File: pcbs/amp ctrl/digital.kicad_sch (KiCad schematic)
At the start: 93 parts

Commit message: Schematic file fix, misc. PCB
Fixed issue with KiCAD's automatic V5→V6 migration (corrected in 6.0.11) that caused problems with component references in multi-channel schematic sheets
Finished migration in amp ctrl PCB, inc. re-assigning "exclude from BOM" attributes to testpoints, solder jumpers
Added mounting hole to amp ctrl PCB for addl support to Ethernet jacks, power connector through stiffener
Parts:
- JP71, TP22, TP23, TP24, TP25, TP26, TP27, TP28, TP29, TP31, TP42, TP43, TP44, TP45, TP46, TP47, TP48, TP49: renamed from ?; now left out of the parts list
- gave numbers to parts that had none: 75

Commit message: New CS amp, misc. layout
Changed current sense amp from INA828 to INA821/819 due to availability: schematic, layout for channel 1 (#6)
Moved some thermistor components & ~Shutdown cap out of the way of the stiffener (#3)
Updated footprints: SOD-323F for slightly larger solderable pads, SOIC-8 to remove excessive length on inside edge
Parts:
- U90: Type (none) -> SMT
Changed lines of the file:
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@@
+      (effects (font (size 1.27 1.27)) hide)
+    )
+    (property "Type" "SMT" (id 8) (at 327.66 158.75 0)
       (effects (font (size 1.27 1.27)) hide)
     )

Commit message: New DAC
Changed DAC from LTC2656 to AD5676 (#5)
Changed digital Vdd for ADC to +3.3V
Removed level translator ICs for +3.3V to +5V; no longer needed because AD5676 has separate analog and digital supply pins
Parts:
- removed JP71: Jumper_NC_Small, Jumper:SolderJumper-2_P1.3mm_Bridged_RoundedPad1.0x1.5mm, symbol amp-ctrl-rescue:Jumper_NC_Small-Device
- removed U8: LTC2656, Martinos:SSOP-20-1EP_4.4x6.5mm_P0.65mm, symbol amp-ctrl-rescue:LTC2656-Martinos
- added C202: 1uF 16V X7R, Capacitor_SMD:C_0603_1608Metric, symbol Device:C
- added R288: 0, Resistor_SMD:R_0805_2012Metric, symbol Device:R
- added U8: AD5676, Don_std:TSSOP-20_4.4x6.5mm_P0.65mm, symbol Don:AD567x
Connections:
- net +5V: no longer C57.2, U90.30 (DVdd)
- net DAC_MISO: now also U8.16 (SDO)
- net DAC_MOSI: now also U8.7 (SDI)
- net DAC_SCKI: now also U8.6 (SCLK)
- net GND: now also C202.1, U8.13 (GND)
- net Vref_Buffered: now also R288.1
- net ~{DAC_CS}: now also U8.5 (~{SYNC})
- net ~{LDAC}: now also U8.15 (~{LDAC})
- net ~{Reset}: now also U8.17 (~{RESET})
- net at R30.1, TP26.1: now also U8.12 (Vout4)
- net at R31.1, TP27.1: now also U8.11 (Vout5)
- net at R32.1, TP28.1: now also U8.10 (Vout6)
- net at R33.1, TP29.1: now also U8.9 (Vout7)
- net at R26.1, TP22.1: now also U8.2 (Vout0)
- net at R27.1, TP23.1: now also U8.1 (Vout1)
- net at R28.1, TP24.1: now also U8.20 (Vout2)
- net at R29.1, TP25.1: now also U8.19 (Vout3)
- net DAC_VCC: no longer names the net of C27.2, C28.2, R21.2
- net DAC_VCC: now also U8.3 (VDD)
- new net: R288.2, U8.18 (VREF)
- new net +3V3: C202.2, C57.2, U8.14 (RSTSEL), U8.4 (VLOGIC), U8.8 (GAIN), U90.30 (DVdd)
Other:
- note added: "GAIN = 1: range is from 0 to 2*Vref RSTSEL = 1: powers up to mid-scale (0A) VREF series resistor allows adding series resistance in case the AD5676R needs to be used due to availability, to limit current draw while the external op-amp and internal Vref buffer "fight" until the internal Vref can be disabled"
- note removed: "PORSEL=1: Resets to mid-scale (0A out) on power-up"
- moved on the sheet: C27, C28, R21

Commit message: DRC fixes
Deleted track stubs and overlapping vias, other misc. DRC fixes (#3)
Shrank width of SOT-563 pads to fall within 0.16 mm clearance (6.3 mils)
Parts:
- J14: footprint Martinos:Shield_Wurth_36107406S_Minimal-inside -> Don:Shield_Wurth_36107406S_Minimal-inside
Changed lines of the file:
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@@
       (effects (font (size 1.27 1.27)) (justify left) hide)
     )
-    (property "Footprint" "Martinos:Shield_Wurth_36107406S_Minimal-inside" (id 2) (at 201.93 120.65 0)
+    (property "Footprint" "Don:Shield_Wurth_36107406S_Minimal-inside" (id 2) (at 201.93 120.65 0)
       (effects (font (size 1.27 1.27)) hide)
     )
@@
   (symbol (lib_id "amp-ctrl-rescue:+3.3V-power") (at 21.59 97.79 90) (mirror x) (unit 1)
     (in_bom yes) (on_board yes)
-    (property "Reference" "#PWR?" (id 0) (at 25.4 97.79 0)
-      (effects (font (size 1.27 1.27)) hide)
-    )
+    (property "Reference" "#PWR0553" (id 0) (at 25.4 97.79 0)
+      (effects (font (size 1.27 1.27)) hide)
+    )

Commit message: Manufacturing fixes for amp control board
Arranged *.Fab text for assembly drawings
Minor stiffener outline fixes, silkscreen fixes
Fixed missing BOM fields on some parts
Removed exported manufacturing files from version control
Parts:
- C26, C31: Manufacturer (none) -> Murata; Part Number (none) -> GRM1885C1H122JA01J
- U6: Type (none) -> SMT
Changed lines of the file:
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@@
   (title_block
     (title "Digital Controls and Voltage Reference")
-    (rev "D3")
+    (date "2023-05-04")
+    (rev "D4")
     (company "Martinos Center @ MGH")
     (comment 1 "Don Straney")
@@
       (effects (font (size 1.27 1.27)) hide)
     )
+    (property "Type" "SMT" (id 8) (at 312.42 96.52 0)
+      (effects (font (size 1.27 1.27)) hide)
+    )
     (pin "1")
     (pin "2")
@@
       (effects (font (size 1.27 1.27)) hide)
     )
-    (property "Manufacturer" "" (id 5) (at 351.79 121.92 0)
+    (property "Manufacturer" "Murata" (id 5) (at 351.79 121.92 0)
       (effects (font (size 1.27 1.27)) hide)
     )
-    (property "Part Number" "" (id 6) (at 351.79 121.92 0)
+    (property "Part Number" "GRM1885C1H122JA01J" (id 6) (at 351.79 121.92 0)
       (effects (font (size 1.27 1.27)) hide)
     )
@@
       (effects (font (size 1.27 1.27)) hide)
     )
-    (property "Manufacturer" "" (id 5) (at 351.79 100.33 0)
+    (property "Manufacturer" "Murata" (id 5) (at 351.79 100.33 0)
       (effects (font (size 1.27 1.27)) hide)
     )
-    (property "Part Number" "" (id 6) (at 351.79 100.33 0)
+    (property "Part Number" "GRM1885C1H122JA01J" (id 6) (at 351.79 100.33 0)
       (effects (font (size 1.27 1.27)) hide)
     )

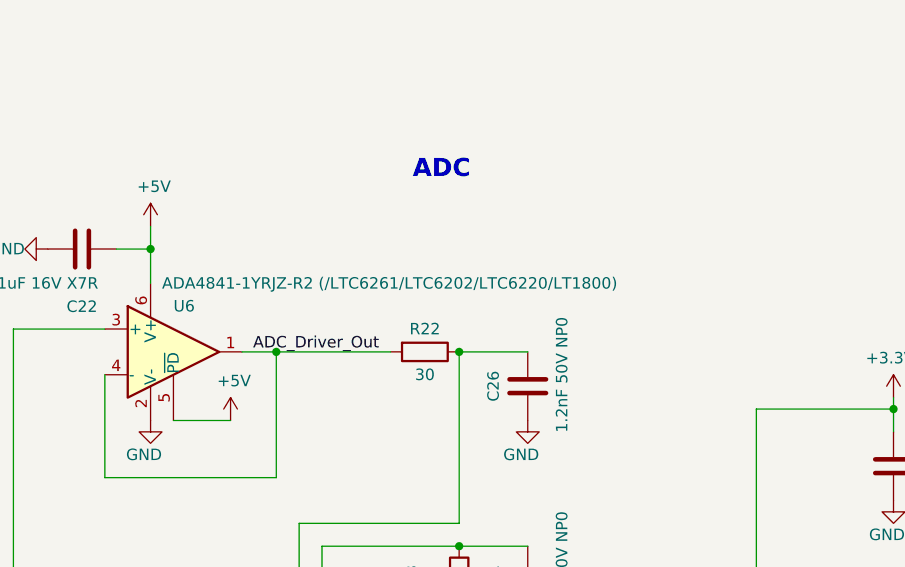
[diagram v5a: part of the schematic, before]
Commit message: Corrected amp board ADC op-amp, created ODU connector 6x7 board
Pared down list of ADC driver op-amps to list of ones tested
Minor fixes to ODU 6x7 connector board (forward-pinned)
Created duplicate of ODU 6x7 connector board, for reverse-pinned
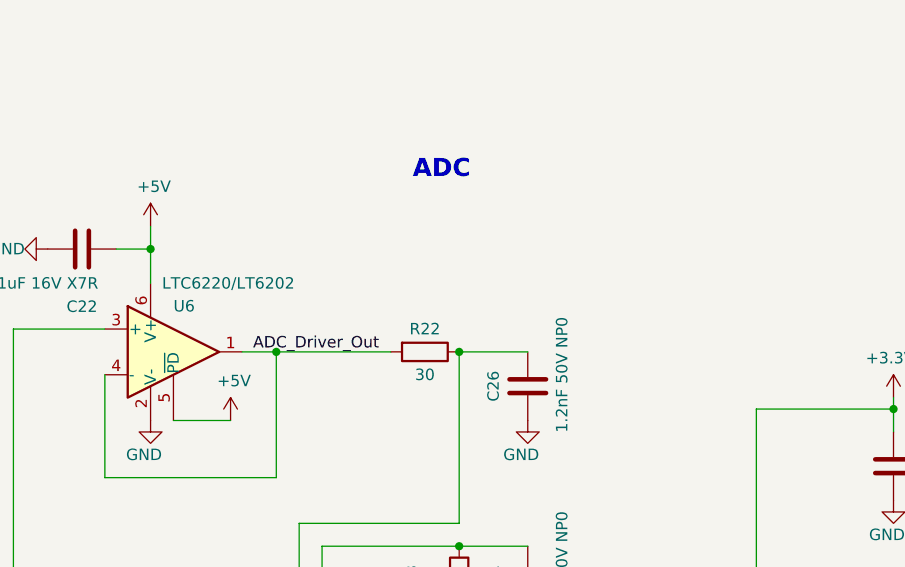
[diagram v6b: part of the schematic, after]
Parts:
- U6: value ADA4841-1YRJZ-R2 (/LTC6261/LTC6202/LTC6220/LT1800) -> LTC6220/LT6202; Part Number ADA4841-1YRJZ-R2 -> LT6220CS5#TRMPBF; Part Number Alt. ADA4841-1YRJZ-R7, LTC6261IS6#TRMPBF, LTC6261HS6#TRMPBF, LTC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 -> LT6220CS5#TRPBF, LT6220IS5#TRMPBF, LT6202HS5#TRMPBF, LT6202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
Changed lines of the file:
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@@
       (effects (font (size 1.27 1.27)) (justify left))
     )
-    (property "Value" "ADA4841-1YRJZ-R2 (/LTC6261/LTC6202/LTC6220/LT1800)" (id 1) (at 311.15 88.9 0)
+    (property "Value" "LTC6220/LT6202" (id 1) (at 311.15 88.9 0)
       (effects (font (size 1.27 1.27)) (justify left))
     )
@@
       (effects (font (size 1.27 1.27)) hide)
     )
-    (property "Part Number" "ADA4841-1YRJZ-R2" (id 5) (at 312.42 96.52 0)
+    (property "Part Number" "LT6220CS5#TRMPBF" (id 5) (at 312.42 96.52 0)
       (effects (font (size 1.27 1.27)) hide)
     )
@@
       (effects (font (size 1.27 1.27)) hide)
     )
-    (property "Part Number Alt." "ADA4841-1YRJZ-R7, LTC6261IS6#TRMPBF, LTC6261HS6#TRMPBF, LTC6261CS6#TRMPBF, LT6202HS5#TRMPBF, LT6202CS5#TRMPBF, LT6202IS5#TRPBF, LT6202IS5#TRMPBF, LT6220CS5#TRMPBF, LT6220CS5#TRPBF, LT6220IS5#TRMPBF, LT1800CS5#TRMPBF, LT1800IS5#TRMPBF, LT1800IS5#TRPBF, LT1800CS5#TRPBF" (id 7) (at 312.42 96.52 0)
+    (property "Part Number Alt." "LT6220CS5#TRPBF, LT6220IS5#TRMPBF, LT6202HS5#TRMPBF, LT6202CS5#TRMPBF, LT6202IS5#TRPBF, LT6202IS5#TRMPBF" (id 7) (at 312.42 96.52 0)
       (effects (font (size 1.27 1.27)) hide)
     )

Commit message: Misc. mfg
Marked top-side testpoints on amp control board as DNP
Updated serial interface board's BOM-placement-help file
Exported stiffener file for amp control board
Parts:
- TP30, TP32, TP60, TP61: DNP (none) -> DNP
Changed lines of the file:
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@@
+      (effects (font (size 1.27 1.27)) hide)
+    )
+    (property "DNP" "DNP" (id 7) (at 363.22 215.9 0)
       (effects (font (size 1.27 1.27)) hide)
     )
@@
     )
     (property "Part Number" "5019" (id 6) (at 374.65 215.9 0)
+      (effects (font (size 1.27 1.27)) hide)
+    )
+    (property "DNP" "DNP" (id 7) (at 374.65 215.9 0)
       (effects (font (size 1.27 1.27)) hide)
     )
@@
       (effects (font (size 1.27 1.27)) hide)
     )
+    (property "DNP" "DNP" (id 7) (at 153.67 153.67 0)
+      (effects (font (size 1.27 1.27)) hide)
+    )
     (pin "1")
   )
@@
       (effects (font (size 1.27 1.27)) hide)
     )
+    (property "DNP" "DNP" (id 7) (at 165.1 153.67 0)
+      (effects (font (size 1.27 1.27)) hide)
+    )

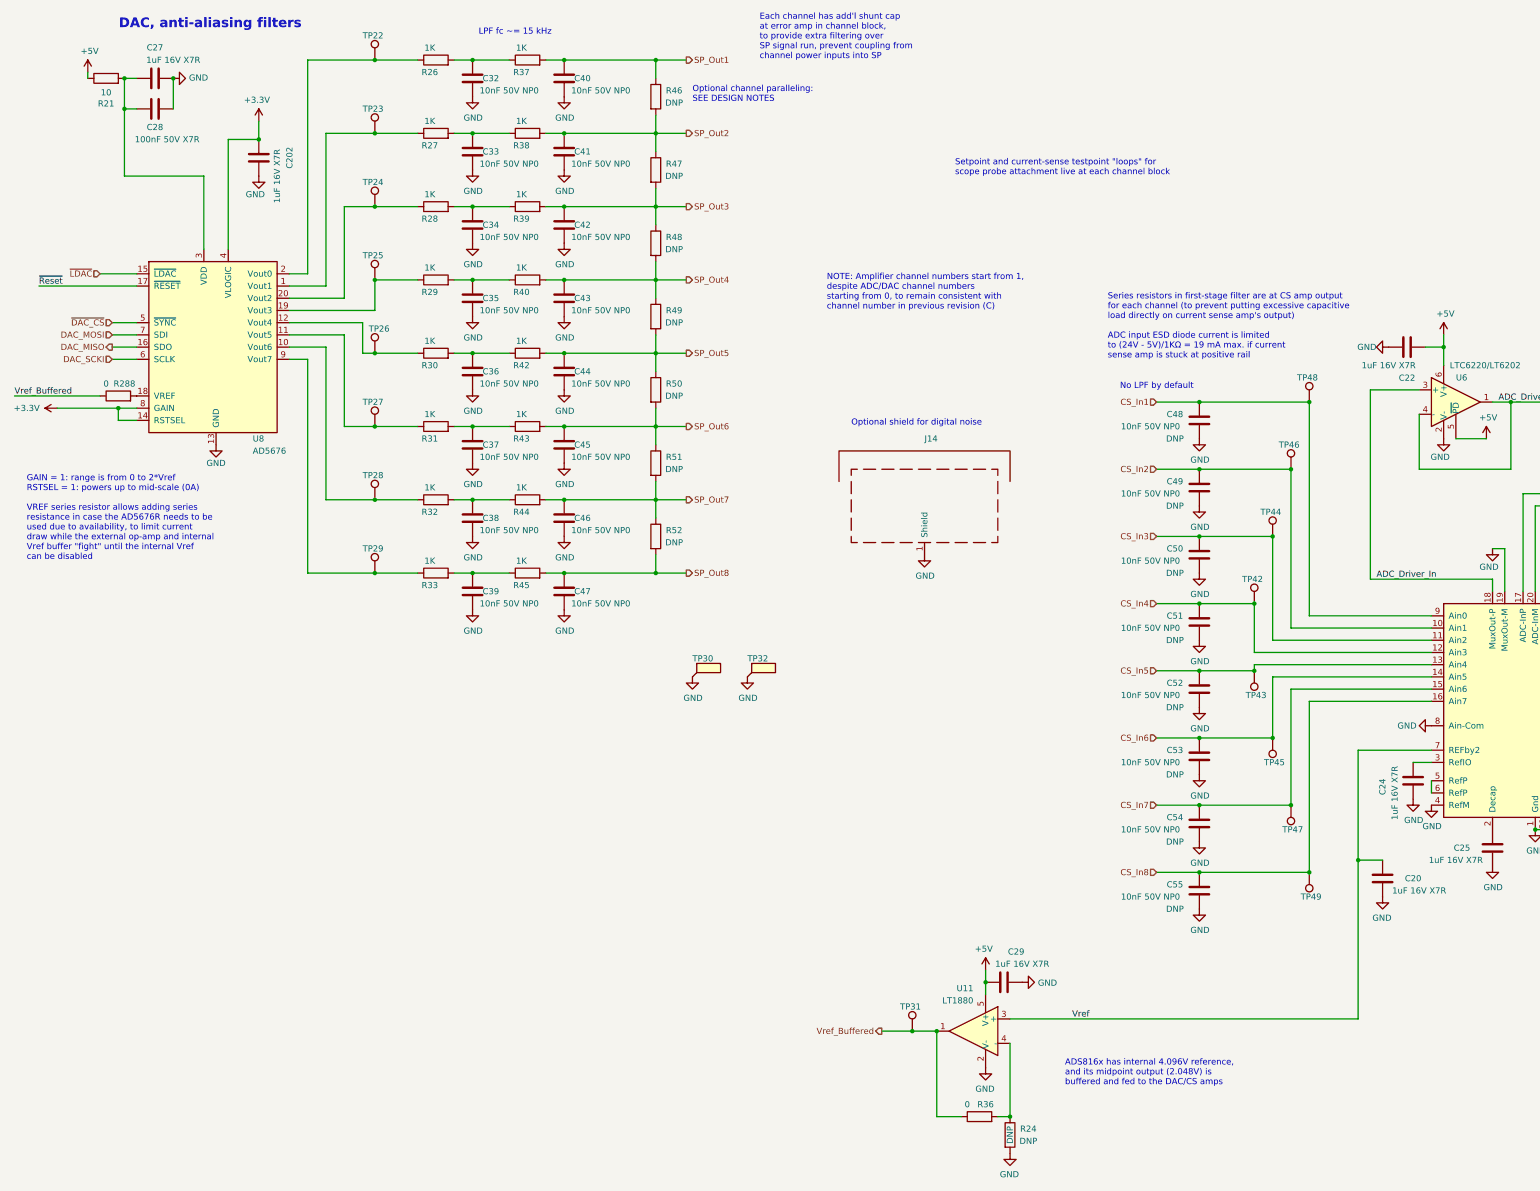
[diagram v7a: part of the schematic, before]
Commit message: Upgraded to KiCAD 7.0 format Added 10µF cap to ADC's REFP pins to fix the voltage reference output (#15) Corrected ADC & DAC reset by adding a separate reset circuit (#14) Increased Cfbk compensation cap on each channel to work out-of-the-box with small coils (#16)
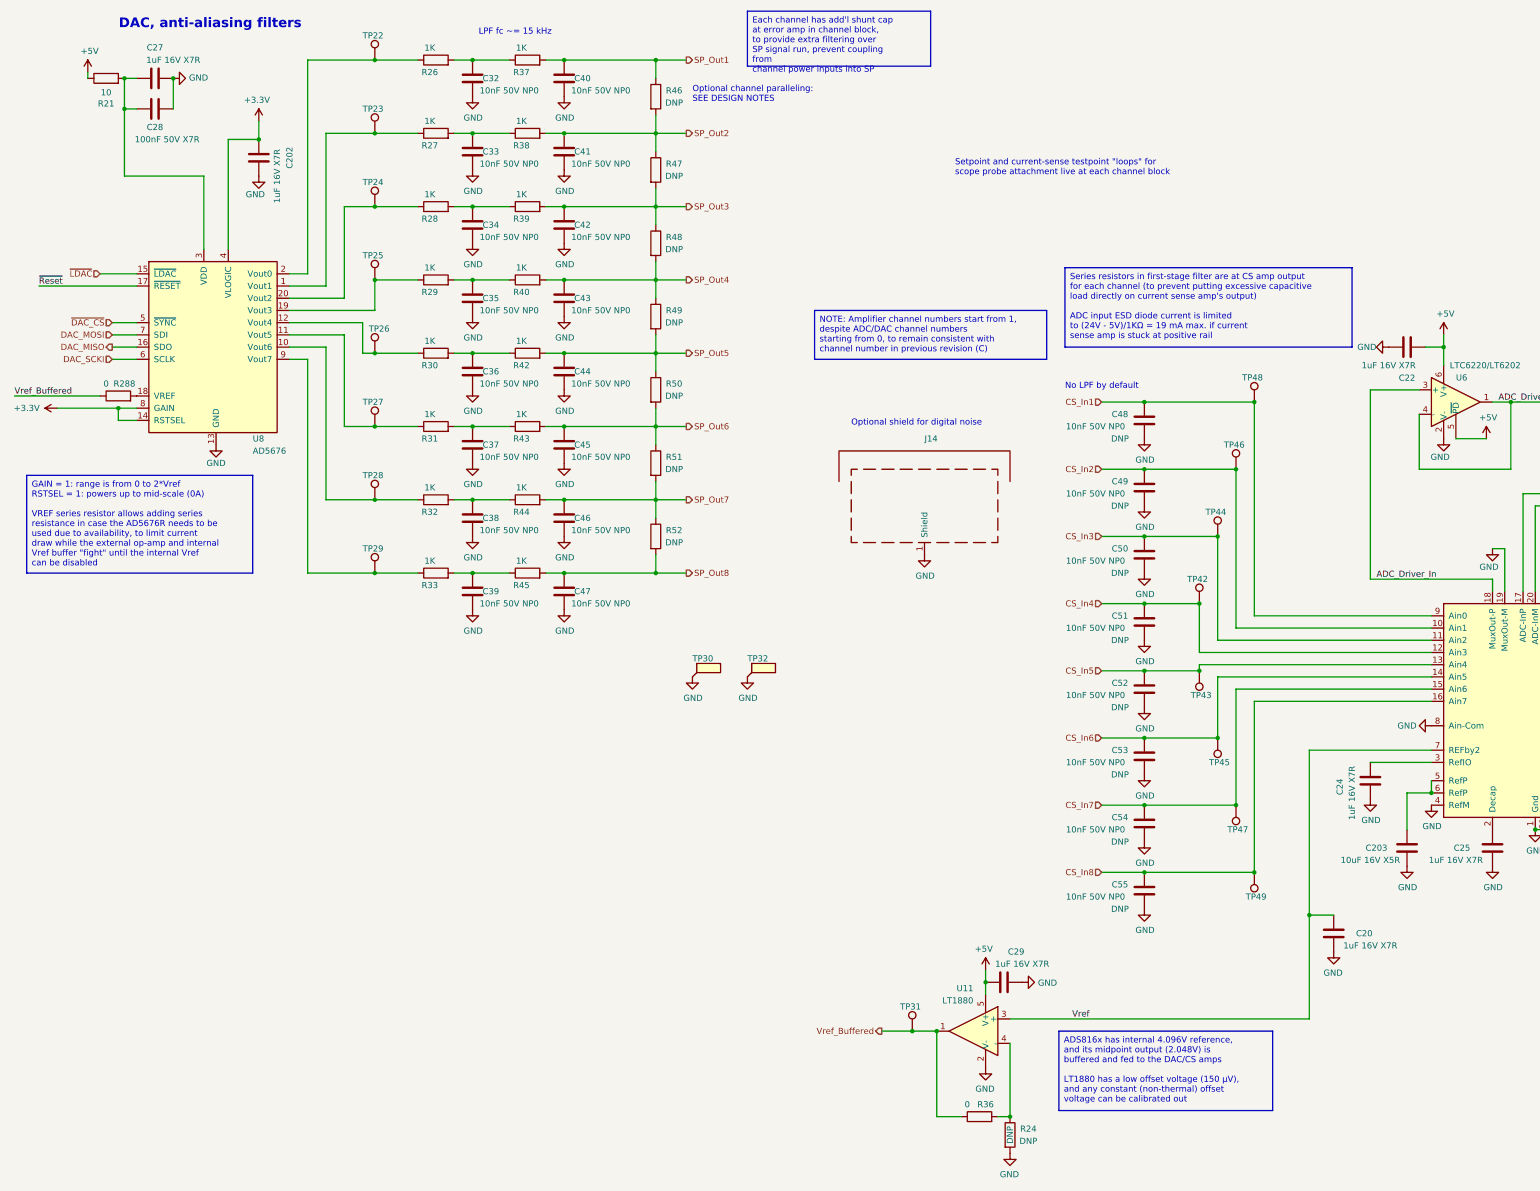
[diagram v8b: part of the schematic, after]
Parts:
- added C203: 10uF 16V X5R, Capacitor_SMD:C_0805_2012Metric, symbol Device:C
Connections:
- net GND: now also C203.2
- net at U90.5 (RefP), U90.6 (RefP): now also C203.1
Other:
- note removed: "ADS816x has internal 4.096V reference, and its midpoint output (2.048V) is buffered and fed to the DAC/CS amps"
- note removed: "Each channel has add'l shunt cap at error amp in channel block, to provide extra filtering over SP signal run, prevent coupling from channel power inputs into SP"
- note removed: "GAIN = 1: range is from 0 to 2*Vref RSTSEL = 1: powers up to mid-scale (0A) VREF series resistor allows adding series resistance in case the AD5676R needs to be used due to availability, to limit current draw while the external op-amp and internal Vref buffer "fight" until the internal Vref can be disabled"
- note removed: "NOTE: Amplifier channel numbers start from 1, despite ADC/DAC channel numbers starting from 0, to remain consistent with channel number in previous revision (C)"
- note removed: "Series resistors in first-stage filter are at CS amp output for each channel (to prevent putting excessive capacitive load directly on current sense amp's output) ADC input ESD diode current is limited to (24V - 5V)/1KΩ = 19 mA max. if current sense amp is stuck at positive rail"
- moved on the sheet: C20, C24, C48, C49, C50, C51, C52, C53, C54, C55, TP42, TP43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
